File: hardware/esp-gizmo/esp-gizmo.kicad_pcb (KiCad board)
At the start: 2 copper layers, 27 parts, among them P1 CONN_01X04, P2 CONN_01X02, P3 CONN_01X03, P4 BOOT JUMPER, P5 CONN_01X04, SW1 SPST, U1 AC-DC, U2 ESP-12E, U3 MOC3021S, U4 MOC3021S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

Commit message: Draft pcb design
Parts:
- added REF***: OSHW-Logo_5.7x6mm_Copper, Symbols:OSHW-Logo_5.7x6mm_Copper, F.Cu at (136.4, 130.6)
- R7, R8, R9, U3, U4, U5: moved to B.Cu
- SW1: moved to F.Cu
- moved R9 38.1 mm to (130.6, 96.5)
- moved U3 33.4 mm to (139.7, 94.0), turned to 90 degrees
- moved U5 29.5 mm to (141.0, 110.5), turned to 90 degrees
- moved P4 26.4 mm to (113.3, 109.7), turned to 90 degrees
- moved R7 23.5 mm to (131.7, 113.0), turned to 0 degrees
- moved U4 23.1 mm to (139.7, 102.2), turned to 90 degrees
- moved R1 16.9 mm to (117.0, 106.3)
- moved R8 16.1 mm to (131.8, 100.7), turned to 270 degrees
- moved R2 13.2 mm to (117.0, 103.8)
- moved R6 11.8 mm to (127.9, 106.2), turned to 0 degrees
- moved P3 11.4 mm to (136.5, 86.6), turned to 270 degrees
- moved R3 10.6 mm to (117.0, 101.2)
- moved R4 10.4 mm to (123.8, 96.5)
- moved R5 10.1 mm to (138.0, 109.1)
- moved P1 10.0 mm to (113.3, 98.7), turned to 0 degrees
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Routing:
- net +3V3: track 0.00 -> 83.1 mm, vias 0 -> 2
- net GND: track 0.00 -> 35.3 mm
- net Net-(R4-Pad2): track 0.00 -> 30.4 mm, vias 0 -> 1
- net Net-(P2-Pad2): track 14.2 -> 36.3 mm
- net Net-(U2-Pad4): track 0.00 -> 20.5 mm, vias 0 -> 1
- net Net-(R3-Pad1): track 0.00 -> 16.4 mm, vias 0 -> 1
- net Net-(P4-Pad1): track 0.00 -> 15.6 mm
- net Net-(P3-Pad2): track 0.00 -> 15.0 mm
- net Net-(U2-Pad20): track 0.00 -> 13.1 mm, vias 0 -> 1
- net Net-(P3-Pad1): track 0.00 -> 11.2 mm
- net Net-(R2-Pad1): track 0.00 -> 10.00 mm, vias 0 -> 1
- net Net-(R6-Pad2): track 0.00 -> 6.35 mm, vias 0 -> 1
- net Net-(U2-Pad19): track 0.00 -> 6.18 mm, vias 0 -> 1
- net Net-(R1-Pad1): track 0.00 -> 5.36 mm, vias 0 -> 1
- net /LOAD_1: track 7.40 -> 12.3 mm
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- added copper zone on B.Cu, net GND
- added copper zone on F.Cu, net GND
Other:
- board outline added: 55.9 x 55.9 mm
- net class Default: trace_width 0.25 -> 0.5
- net class hi_voltage added: clearance 0.5, trace_width 0.5, via_dia 0.6, via_drill 0.4
- net class load: trace_width 1.5 -> 1.2

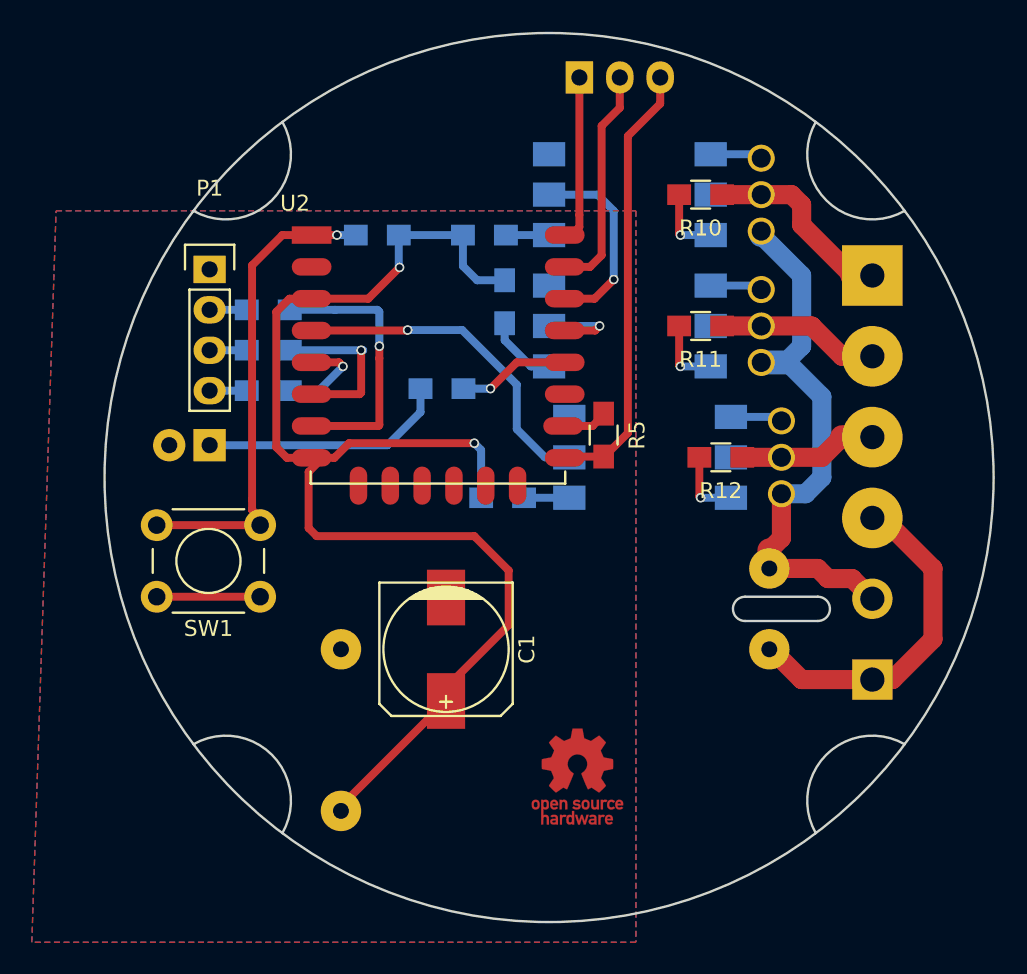
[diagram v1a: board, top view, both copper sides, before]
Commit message: Some fixes of schematic and board
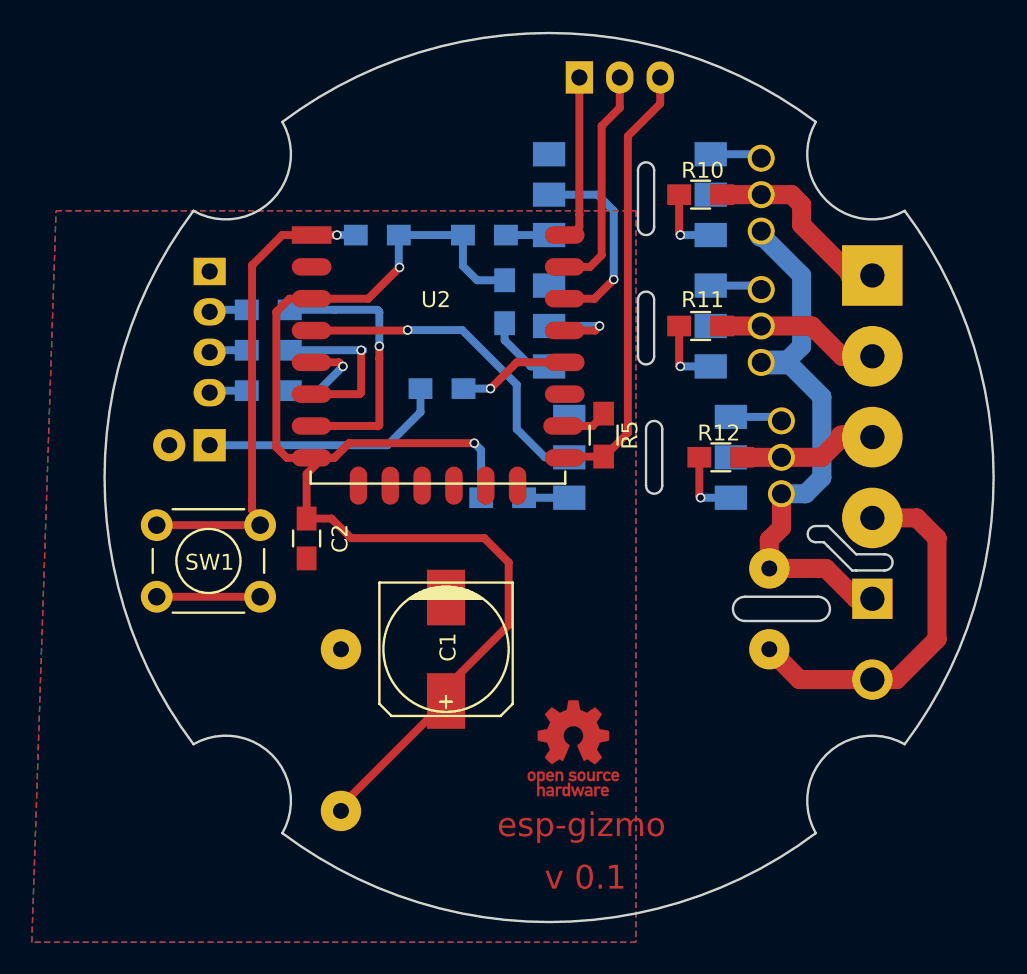
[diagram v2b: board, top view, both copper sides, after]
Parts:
- added C2: 100n, Capacitors_SMD:C_0805_HandSoldering, F.Cu at (119.4, 115.6)
- P1: moved to B.Cu
- moved REF*** 1.80 mm to (136.1, 128.8)
- moved P1 0.13 mm to (113.3, 98.8), turned to 180 degrees
- turned P2 to 270 degrees
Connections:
- P5 pad 4: Net-(P2-Pad1) -> Net-(P2-Pad2)
- U1 pad 1: Net-(P2-Pad2) -> Net-(P2-Pad1)
- U1 pad 2: Net-(P2-Pad1) -> Net-(P2-Pad2)
- U6 pad 1: Net-(P2-Pad2) -> Net-(P2-Pad1)
- U7 pad 1: Net-(P2-Pad2) -> Net-(P2-Pad1)
- U8 pad 1: Net-(P2-Pad2) -> Net-(P2-Pad1)
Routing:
- net Net-(P2-Pad1): track 21.7 -> 36.3 mm
- net Net-(P2-Pad2): track 36.3 -> 24.1 mm
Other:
- outline, holes or cut-outs redrawn
- board text added: "esp-gizmo"
- board text added: "v 0.1"

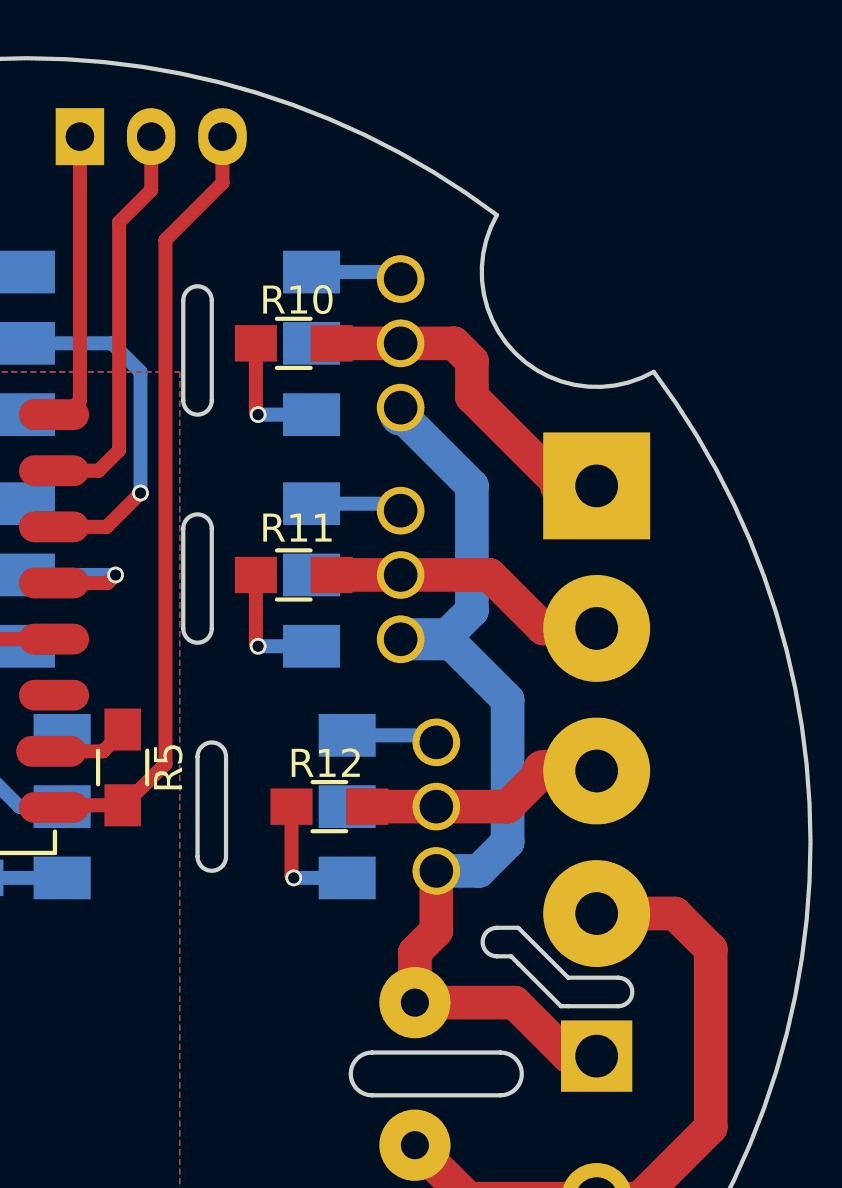
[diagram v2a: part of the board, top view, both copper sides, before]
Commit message: Schematic: switch to zero crossing opto-coupler
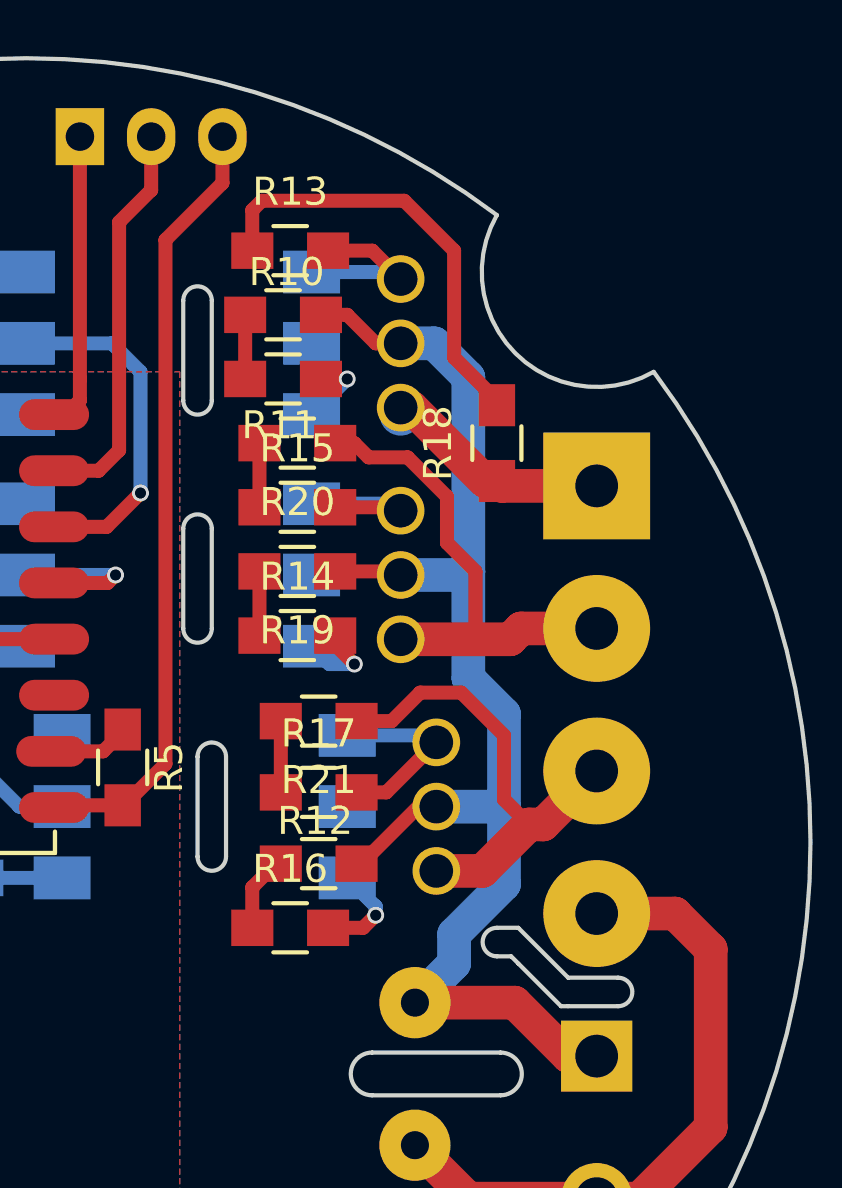
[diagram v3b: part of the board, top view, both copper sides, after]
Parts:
- added R13: 160, Resistors_SMD:R_0805_HandSoldering, F.Cu at (144.0, 90.7)
- added R14: 160, Resistors_SMD:R_0805_HandSoldering, F.Cu at (144.3, 104.4)
- added R15: 160, Resistors_SMD:R_0805_HandSoldering, F.Cu at (144.3, 99.8)
- added R16: 160, Resistors_SMD:R_0805_HandSoldering, F.Cu at (144.0, 114.8)
- added R17: 160, Resistors_SMD:R_0805_HandSoldering, F.Cu at (145.0, 110.0)
- added R18: 160, Resistors_SMD:R_0805_HandSoldering, F.Cu at (151.4, 97.5)
- added R19: 160, Resistors_SMD:R_0805_HandSoldering, F.Cu at (144.3, 102.1)
- added R20: 160, Resistors_SMD:R_0805_HandSoldering, F.Cu at (144.3, 97.5)
- added R21: 160, Resistors_SMD:R_0805_HandSoldering, F.Cu at (145.0, 107.4)
- R10, R11, R12: value 180 -> 160
- R7, R8, R9: value 1k -> 430
- U3, U4, U5: value MOC3021S -> MOC3063
- moved R11 7.00 mm to (143.8, 95.2), turned to 0 degrees
- moved R12 2.07 mm to (145.0, 112.5)
- moved R10 1.09 mm to (143.8, 93.0)
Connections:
- net Net-(P2-Pad2) renamed /COMMON
- P5 pad 1: /LOAD_1 -> /LOAD1
- P5 pad 2: /LOAD_2 -> /LOAD2
- P5 pad 3: /LOAD_3 -> /LOAD3
- R10 pad 1: /LOAD_1 -> Net-(P2-Pad1)
- R11 pad 1: /LOAD_2 -> Net-(R10-Pad2)
- R12 pad 1: /LOAD_3 -> Net-(P2-Pad1)
- U3 pad 6: Net-(R10-Pad2) -> Net-(R11-Pad2)
- U4 pad 6: Net-(R11-Pad2) -> Net-(R14-Pad2)
- U5 pad 6: Net-(R12-Pad2) -> Net-(R16-Pad2)
- U6 pad 1: Net-(P2-Pad1) -> /LOAD1
- U6 pad 2: /LOAD_1 -> Net-(P2-Pad1)
- U7 pad 1: Net-(P2-Pad1) -> /LOAD2
- U7 pad 2: /LOAD_2 -> Net-(P2-Pad1)
- U8 pad 1: Net-(P2-Pad1) -> /LOAD3
- U8 pad 2: /LOAD_3 -> Net-(P2-Pad1)
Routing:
- net /LOAD2: track 0.00 -> 17.4 mm
- net /LOAD3: track 0.00 -> 17.0 mm
- net Net-(R13-Pad1): track 0.00 -> 15.7 mm
- net /LOAD_1: track 12.3 -> 0.00 mm
- net Net-(P2-Pad1): track 36.3 -> 48.5 mm
- net /LOAD_2: track 10.2 -> 0.00 mm
- net /LOAD1: track 0.00 -> 9.66 mm
- net /LOAD_3: track 8.70 -> 0.00 mm
- net Net-(R16-Pad2): track 0.00 -> 3.63 mm, vias 0 -> 1
- net Net-(R17-Pad2): track 3.28 -> 6.86 mm
- net Net-(R14-Pad2): track 0.00 -> 3.09 mm, vias 0 -> 1
- net Net-(R13-Pad2): track 3.28 -> 6.28 mm
- net Net-(R17-Pad1): track 0.00 -> 2.54 mm
- net Net-(R15-Pad2): track 3.28 -> 5.66 mm
- net Net-(R15-Pad1): track 0.00 -> 2.29 mm
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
